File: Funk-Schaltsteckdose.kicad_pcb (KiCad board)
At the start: 2 copper layers, 61 x 96.5 mm, 20 parts, among them J1 L, J2 L', J3 N, K1 G6B-2214P, Q1 BC337, SW1 SW_DIP_x01, U1 ArduinoProMini, U2 LP2950-3.3_TO92, U4 E07_868MS10

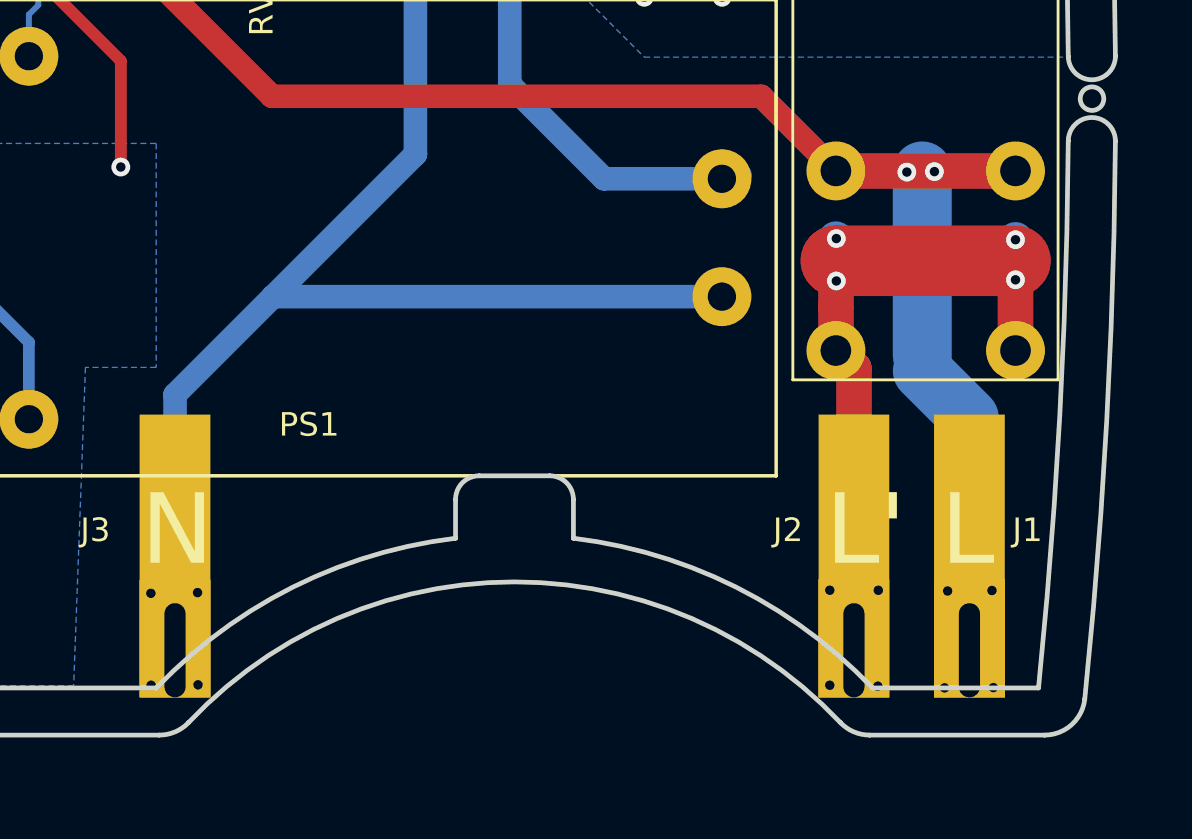
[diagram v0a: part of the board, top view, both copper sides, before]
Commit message: Revert "Layout angepasst"
This reverts commit ff7744db74a23c470d7ae99f610fa08b87265f2a.
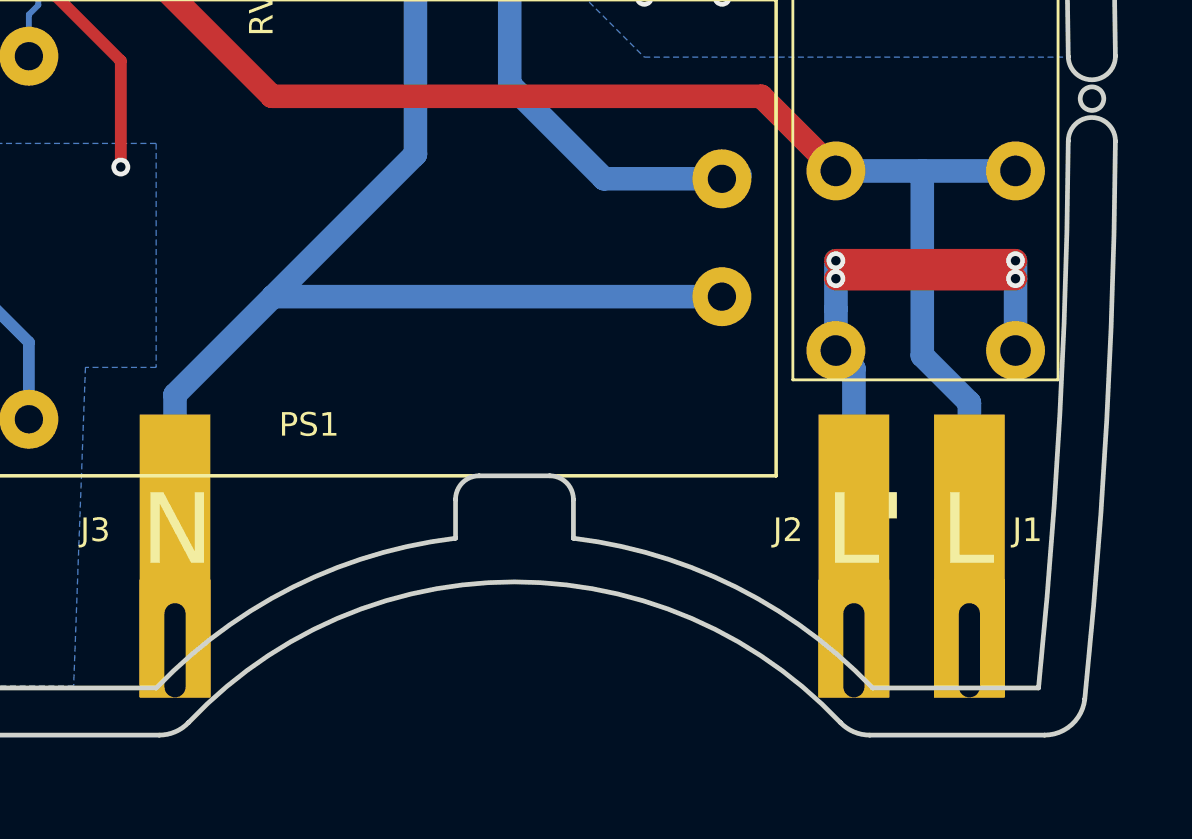
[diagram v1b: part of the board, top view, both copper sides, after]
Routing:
- net Net-(J2-Pad1): track 44.1 -> 32.5 mm, vias 8 -> 4
- net Net-(F1-Pad2): track 61.6 -> 60.4 mm, vias 6 -> 0
- net Net-(J3-Pad1): vias 4 -> 0
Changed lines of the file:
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@@
     (thickness 1.6)
     (drawings 86)
-    (tracks 221)
+    (tracks 198)
     (zones 0)
     (modules 20)
@@
   (gr_line (start 86.03 90.475) (end 86.03 76.505) (layer Edge.Cuts) (width 0.15))
   (gr_line (start 83.49 76.505) (end 83.49 90.475) (layer Edge.Cuts) (width 0.15))
-  (via (at 84.575 148.985) (size 0.8) (drill 0.4) (layers F.Cu B.Cu) (net 8))
-  (via (at 86.555 148.955) (size 0.8) (drill 0.4) (layers F.Cu B.Cu) (net 8))
-  (via (at 86.575 152.865) (size 0.8) (drill 0.4) (layers F.Cu B.Cu) (net 8))
-  (via (at 84.585 152.885) (size 0.8) (drill 0.4) (layers F.Cu B.Cu) (net 8))
-  (via (at 115.435 148.855) (size 0.8) (drill 0.4) (layers F.Cu B.Cu) (net 2))
-  (via (at 115.415 152.925) (size 0.8) (drill 0.4) (layers F.Cu B.Cu) (net 2))
-  (via (at 113.375 152.885) (size 0.8) (drill 0.4) (layers F.Cu B.Cu) (net 2))
-  (via (at 118.245 152.995) (size 0.8) (drill 0.4) (layers F.Cu B.Cu) (net 7))
-  (via (at 120.315 152.985) (size 0.8) (drill 0.4) (layers F.Cu B.Cu) (net 7))
-  (via (at 120.255 148.865) (size 0.8) (drill 0.4) (layers F.Cu B.Cu) (net 7))
-  (via (at 118.375 148.885) (size 0.8) (drill 0.4) (layers F.Cu B.Cu) (net 7))
   (segment (start 109.41 131.4) (end 109.571 131.239) (width 1) (layer B.Cu) (net 1))
   (segment (start 82.8 115.9) (end 86.3 119.4) (width 1) (layer B.Cu) (net 1))
@@
   (segment (start 90.8 119.4) (end 96.3 119.4) (width 1) (layer B.Cu) (net 1))
   (segment (start 96.3 119.4) (end 99.8 122.9) (width 1) (layer B.Cu) (net 1))
-  (segment (start 113.635 138.685) (end 114.4 139.45) (width 1.5) (layer B.Cu) (net 2))
-  (segment (start 114.4 139.45) (end 114.4 148) (width 1.5) (layer B.Cu) (net 2))
-  (segment (start 113.635 134.875) (end 113.655 134.875) (width 3) (layer F.Cu) (net 2))
-  (segment (start 113.635 138.685) (end 113.635 136.835) (width 1.5) (layer F.Cu) (net 2))
-  (segment (start 121.255 138.685) (end 121.255 136.135) (width 1.5) (layer F.Cu) (net 2))
-  (via (at 113.375 148.855) (size 0.8) (drill 0.4) (layers F.Cu B.Cu) (net 2))
-  (segment (start 113.635 138.685) (end 113.635 138.715) (width 1) (layer F.Cu) (net 2))
-  (segment (start 113.635 138.715) (end 114.405 139.485) (width 1.5) (layer F.Cu) (net 2))
-  (segment (start 113.655 134.875) (end 121.255 134.875) (width 3) (layer F.Cu) (net 2))
-  (via (at 113.655 133.935) (size 0.8) (drill 0.4) (layers F.Cu B.Cu) (net 2))
-  (segment (start 121.255 134.885) (end 121.255 134.875) (width 1.5) (layer F.Cu) (net 2))
-  (via (at 121.255 133.985) (size 0.8) (drill 0.4) (layers F.Cu B.Cu) (net 2))
-  (segment (start 121.255 136.135) (end 121.255 134.885) (width 1.5) (layer F.Cu) (net 2))
-  (via (at 121.255 135.685) (size 0.8) (drill 0.4) (layers F.Cu B.Cu) (net 2))
-  (segment (start 113.655 134.875) (end 113.655 134.875) (width 3) (layer F.Cu) (net 2))
-  (via (at 113.655 135.735) (size 0.8) (drill 0.4) (layers F.Cu B.Cu) (net 2))
-  (segment (start 113.635 136.835) (end 113.635 134.875) (width 1.5) (layer F.Cu) (net 2))
-  (segment (start 113.635 133.955) (end 113.655 133.935) (width 1) (layer B.Cu) (net 2))
-  (segment (start 113.635 138.685) (end 113.635 133.955) (width 1.5) (layer B.Cu) (net 2))
-  (segment (start 121.255 138.685) (end 121.255 133.985) (width 1.5) (layer B.Cu) (net 2))
-  (segment (start 114.4 139.45) (end 114.4 148.15) (width 1.5) (layer F.Cu) (net 2))
+  (segment (start 121.255 138.685) (end 121.255 135.637) (width 1) (layer B.Cu) (net 2))
+  (segment (start 113.635 138.685) (end 114.4 139.45) (width 1) (layer B.Cu) (net 2))
+  (segment (start 114.4 139.45) (end 114.4 148) (width 1) (layer B.Cu) (net 2))
+  (segment (start 113.635 138.685) (end 113.635 136.917234) (width 1) (layer B.Cu) (net 2))
+  (segment (start 113.635 136.917234) (end 113.635 135.637) (width 1) (layer B.Cu) (net 2))
+  (segment (start 113.635 134.875) (end 113.635 134.875) (width 1) (layer B.Cu) (net 2))
+  (via (at 113.635 134.875) (size 0.8) (drill 0.4) (layers F.Cu B.Cu) (net 2))
+  (via (at 121.255 134.875) (size 0.8) (drill 0.4) (layers F.Cu B.Cu) (net 2))
+  (segment (start 113.635 135.637) (end 113.635 134.875) (width 1) (layer B.Cu) (net 2))
+  (via (at 113.635 135.637) (size 0.8) (drill 0.4) (layers F.Cu B.Cu) (net 2))
+  (segment (start 121.255 135.637) (end 121.255 134.875) (width 1) (layer B.Cu) (net 2))
+  (via (at 121.255 135.637) (size 0.8) (drill 0.4) (layers F.Cu B.Cu) (net 2))
+  (segment (start 113.635 134.875) (end 121.255 134.875) (width 1) (layer F.Cu) (net 2))
+  (segment (start 113.635 135.637) (end 121.255 135.637) (width 1) (layer F.Cu) (net 2))
   (segment (start 105.08 92.38) (end 106.35 93.65) (width 0.25) (layer B.Cu) (net 3))
   (segment (start 105.08 91.279029) (end 105.08 92.38) (width 0.25) (layer B.Cu) (net 3))
@@
   (segment (start 82.79 120.98) (end 89.71 127.9) (width 1) (layer F.Cu) (net 7))
   (segment (start 89.71 127.9) (end 110.47 127.9) (width 1) (layer F.Cu) (net 7))
-  (segment (start 117.3 131.065) (end 117.3 131.065) (width 2.5) (layer B.Cu) (net 7))
-  (segment (start 117.3 131.065) (end 121.255 131.065) (width 1.5) (layer B.Cu) (net 7))
-  (segment (start 113.635 131.065) (end 117.3 131.065) (width 1.5) (layer B.Cu) (net 7))
-  (segment (start 113.635 131.065) (end 121.255 131.065) (width 1.5) (layer F.Cu) (net 7))
-  (segment (start 117.3 131.065) (end 117.3 138.9) (width 2.5) (layer B.Cu) (net 7))
-  (via (at 116.645 131.115) (size 0.8) (drill 0.4) (layers F.Cu B.Cu) (net 7))
-  (segment (start 117.3 131.065) (end 117.3 131.065) (width 2.5) (layer B.Cu) (net 7))
-  (via (at 117.815 131.095) (size 0.8) (drill 0.4) (layers F.Cu B.Cu) (net 7))
-  (segment (start 117.3 139.55) (end 117.3 138.9) (width 1) (layer B.Cu) (net 7))
-  (segment (start 119.3 141.55) (end 117.3 139.55) (width 2.5) (layer B.Cu) (net 7))
+  (segment (start 117.3 131.065) (end 117.3 138.9) (width 1) (layer B.Cu) (net 7))
+  (segment (start 117.3 131.065) (end 121.255 131.065) (width 1) (layer B.Cu) (net 7))
+  (segment (start 113.635 131.065) (end 117.3 131.065) (width 1) (layer B.Cu) (net 7))
+  (segment (start 119.3 140.9) (end 119.3 148) (width 1) (layer B.Cu) (net 7))
+  (segment (start 117.3 138.9) (end 119.3 140.9) (width 1) (layer B.Cu) (net 7))
   (segment (start 85.6 140.558) (end 85.6 148) (width 1) (layer B.Cu) (net 8))
   (segment (start 108.8 136.4) (end 89.758 136.4) (width 1) (layer B.Cu) (net 8))

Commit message: Layout angepasst
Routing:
- net Net-(J2-Pad1): track 32.5 -> 44.1 mm, vias 4 -> 8
- net Net-(F1-Pad2): track 60.4 -> 61.6 mm, vias 0 -> 6
- net Net-(J3-Pad1): vias 0 -> 4
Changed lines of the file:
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@@
     (thickness 1.6)
     (drawings 86)
-    (tracks 198)
+    (tracks 221)
     (zones 0)
     (modules 20)
@@
   (gr_line (start 86.03 90.475) (end 86.03 76.505) (layer Edge.Cuts) (width 0.15))
   (gr_line (start 83.49 76.505) (end 83.49 90.475) (layer Edge.Cuts) (width 0.15))
+  (via (at 84.575 148.985) (size 0.8) (drill 0.4) (layers F.Cu B.Cu) (net 8))
+  (via (at 86.555 148.955) (size 0.8) (drill 0.4) (layers F.Cu B.Cu) (net 8))
+  (via (at 86.575 152.865) (size 0.8) (drill 0.4) (layers F.Cu B.Cu) (net 8))
+  (via (at 84.585 152.885) (size 0.8) (drill 0.4) (layers F.Cu B.Cu) (net 8))
+  (via (at 115.435 148.855) (size 0.8) (drill 0.4) (layers F.Cu B.Cu) (net 2))
+  (via (at 115.415 152.925) (size 0.8) (drill 0.4) (layers F.Cu B.Cu) (net 2))
+  (via (at 113.375 152.885) (size 0.8) (drill 0.4) (layers F.Cu B.Cu) (net 2))
+  (via (at 118.245 152.995) (size 0.8) (drill 0.4) (layers F.Cu B.Cu) (net 7))
+  (via (at 120.315 152.985) (size 0.8) (drill 0.4) (layers F.Cu B.Cu) (net 7))
+  (via (at 120.255 148.865) (size 0.8) (drill 0.4) (layers F.Cu B.Cu) (net 7))
+  (via (at 118.375 148.885) (size 0.8) (drill 0.4) (layers F.Cu B.Cu) (net 7))
   (segment (start 109.41 131.4) (end 109.571 131.239) (width 1) (layer B.Cu) (net 1))
   (segment (start 82.8 115.9) (end 86.3 119.4) (width 1) (layer B.Cu) (net 1))
@@
   (segment (start 90.8 119.4) (end 96.3 119.4) (width 1) (layer B.Cu) (net 1))
   (segment (start 96.3 119.4) (end 99.8 122.9) (width 1) (layer B.Cu) (net 1))
-  (segment (start 121.255 138.685) (end 121.255 135.637) (width 1) (layer B.Cu) (net 2))
-  (segment (start 113.635 138.685) (end 114.4 139.45) (width 1) (layer B.Cu) (net 2))
-  (segment (start 114.4 139.45) (end 114.4 148) (width 1) (layer B.Cu) (net 2))
-  (segment (start 113.635 138.685) (end 113.635 136.917234) (width 1) (layer B.Cu) (net 2))
-  (segment (start 113.635 136.917234) (end 113.635 135.637) (width 1) (layer B.Cu) (net 2))
-  (segment (start 113.635 134.875) (end 113.635 134.875) (width 1) (layer B.Cu) (net 2))
-  (via (at 113.635 134.875) (size 0.8) (drill 0.4) (layers F.Cu B.Cu) (net 2))
-  (via (at 121.255 134.875) (size 0.8) (drill 0.4) (layers F.Cu B.Cu) (net 2))
-  (segment (start 113.635 135.637) (end 113.635 134.875) (width 1) (layer B.Cu) (net 2))
-  (via (at 113.635 135.637) (size 0.8) (drill 0.4) (layers F.Cu B.Cu) (net 2))
-  (segment (start 121.255 135.637) (end 121.255 134.875) (width 1) (layer B.Cu) (net 2))
-  (via (at 121.255 135.637) (size 0.8) (drill 0.4) (layers F.Cu B.Cu) (net 2))
-  (segment (start 113.635 134.875) (end 121.255 134.875) (width 1) (layer F.Cu) (net 2))
-  (segment (start 113.635 135.637) (end 121.255 135.637) (width 1) (layer F.Cu) (net 2))
+  (segment (start 113.635 138.685) (end 114.4 139.45) (width 1.5) (layer B.Cu) (net 2))
+  (segment (start 114.4 139.45) (end 114.4 148) (width 1.5) (layer B.Cu) (net 2))
+  (segment (start 113.635 134.875) (end 113.655 134.875) (width 3) (layer F.Cu) (net 2))
+  (segment (start 113.635 138.685) (end 113.635 136.835) (width 1.5) (layer F.Cu) (net 2))
+  (segment (start 121.255 138.685) (end 121.255 136.135) (width 1.5) (layer F.Cu) (net 2))
+  (via (at 113.375 148.855) (size 0.8) (drill 0.4) (layers F.Cu B.Cu) (net 2))
+  (segment (start 113.635 138.685) (end 113.635 138.715) (width 1) (layer F.Cu) (net 2))
+  (segment (start 113.635 138.715) (end 114.405 139.485) (width 1.5) (layer F.Cu) (net 2))
+  (segment (start 113.655 134.875) (end 121.255 134.875) (width 3) (layer F.Cu) (net 2))
+  (via (at 113.655 133.935) (size 0.8) (drill 0.4) (layers F.Cu B.Cu) (net 2))
+  (segment (start 121.255 134.885) (end 121.255 134.875) (width 1.5) (layer F.Cu) (net 2))
+  (via (at 121.255 133.985) (size 0.8) (drill 0.4) (layers F.Cu B.Cu) (net 2))
+  (segment (start 121.255 136.135) (end 121.255 134.885) (width 1.5) (layer F.Cu) (net 2))
+  (via (at 121.255 135.685) (size 0.8) (drill 0.4) (layers F.Cu B.Cu) (net 2))
+  (segment (start 113.655 134.875) (end 113.655 134.875) (width 3) (layer F.Cu) (net 2))
+  (via (at 113.655 135.735) (size 0.8) (drill 0.4) (layers F.Cu B.Cu) (net 2))
+  (segment (start 113.635 136.835) (end 113.635 134.875) (width 1.5) (layer F.Cu) (net 2))
+  (segment (start 113.635 133.955) (end 113.655 133.935) (width 1) (layer B.Cu) (net 2))
+  (segment (start 113.635 138.685) (end 113.635 133.955) (width 1.5) (layer B.Cu) (net 2))
+  (segment (start 121.255 138.685) (end 121.255 133.985) (width 1.5) (layer B.Cu) (net 2))
+  (segment (start 114.4 139.45) (end 114.4 148.15) (width 1.5) (layer F.Cu) (net 2))
   (segment (start 105.08 92.38) (end 106.35 93.65) (width 0.25) (layer B.Cu) (net 3))
   (segment (start 105.08 91.279029) (end 105.08 92.38) (width 0.25) (layer B.Cu) (net 3))
@@
   (segment (start 82.79 120.98) (end 89.71 127.9) (width 1) (layer F.Cu) (net 7))
   (segment (start 89.71 127.9) (end 110.47 127.9) (width 1) (layer F.Cu) (net 7))
-  (segment (start 117.3 131.065) (end 117.3 138.9) (width 1) (layer B.Cu) (net 7))
-  (segment (start 117.3 131.065) (end 121.255 131.065) (width 1) (layer B.Cu) (net 7))
-  (segment (start 113.635 131.065) (end 117.3 131.065) (width 1) (layer B.Cu) (net 7))
-  (segment (start 119.3 140.9) (end 119.3 148) (width 1) (layer B.Cu) (net 7))
-  (segment (start 117.3 138.9) (end 119.3 140.9) (width 1) (layer B.Cu) (net 7))
+  (segment (start 117.3 131.065) (end 117.3 131.065) (width 2.5) (layer B.Cu) (net 7))
+  (segment (start 117.3 131.065) (end 121.255 131.065) (width 1.5) (layer B.Cu) (net 7))
+  (segment (start 113.635 131.065) (end 117.3 131.065) (width 1.5) (layer B.Cu) (net 7))
+  (segment (start 113.635 131.065) (end 121.255 131.065) (width 1.5) (layer F.Cu) (net 7))
+  (segment (start 117.3 131.065) (end 117.3 138.9) (width 2.5) (layer B.Cu) (net 7))
+  (via (at 116.645 131.115) (size 0.8) (drill 0.4) (layers F.Cu B.Cu) (net 7))
+  (segment (start 117.3 131.065) (end 117.3 131.065) (width 2.5) (layer B.Cu) (net 7))
+  (via (at 117.815 131.095) (size 0.8) (drill 0.4) (layers F.Cu B.Cu) (net 7))
+  (segment (start 117.3 139.55) (end 117.3 138.9) (width 1) (layer B.Cu) (net 7))
+  (segment (start 119.3 141.55) (end 117.3 139.55) (width 2.5) (layer B.Cu) (net 7))
   (segment (start 85.6 140.558) (end 85.6 148) (width 1) (layer B.Cu) (net 8))
   (segment (start 108.8 136.4) (end 89.758 136.4) (width 1) (layer B.Cu) (net 8))
